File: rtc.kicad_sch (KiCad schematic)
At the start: 8 parts, among them U1501 PCF85063ATL, Y1501 32.768kHz 7pF

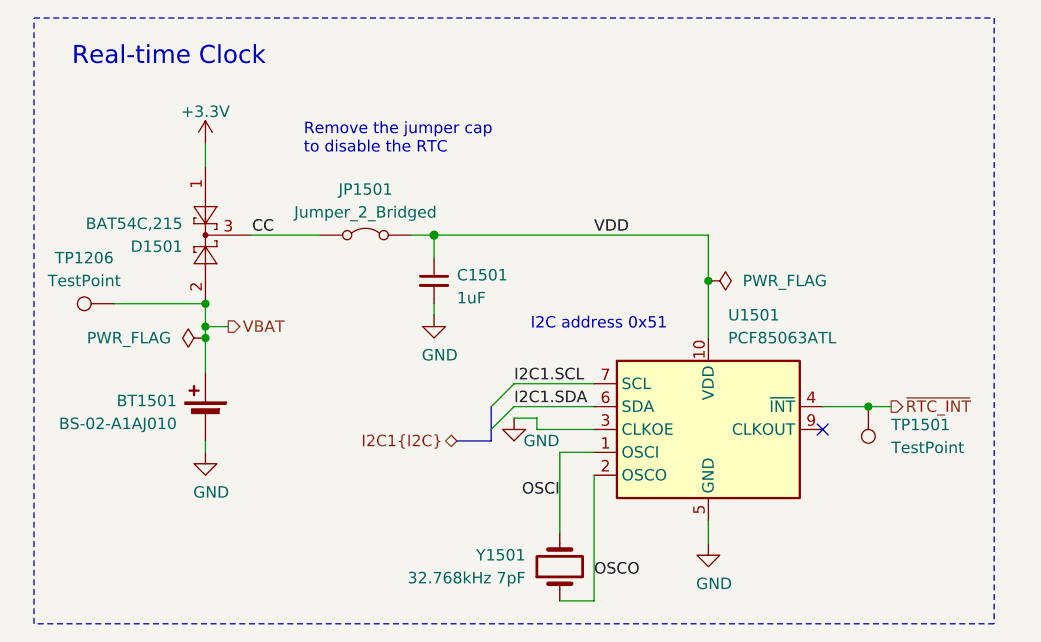
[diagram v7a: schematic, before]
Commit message: Change MCU to RP2040
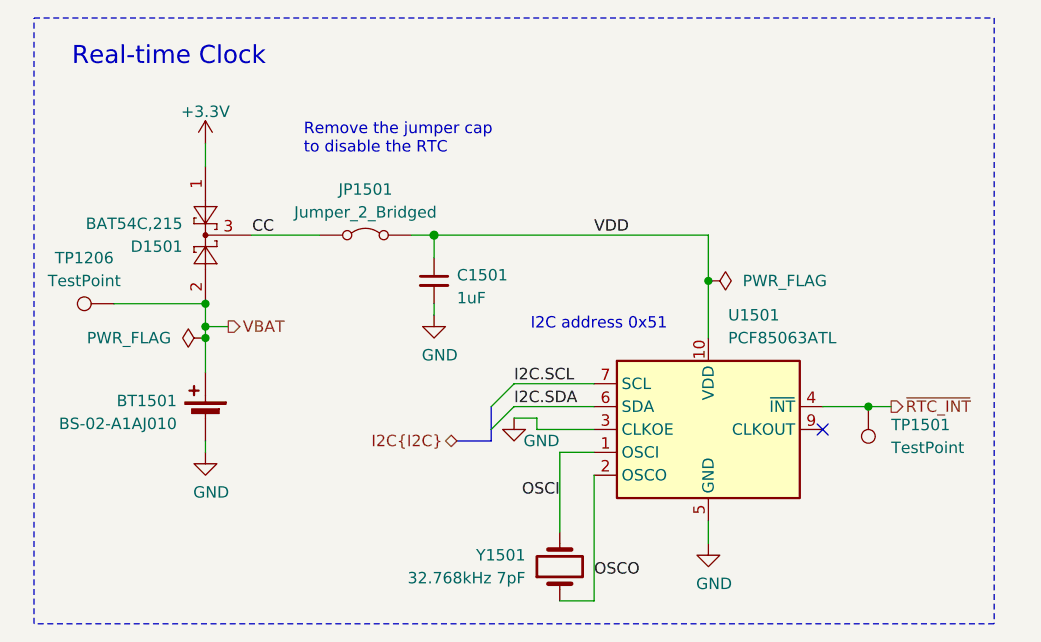
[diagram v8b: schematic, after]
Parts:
- JP1501: footprint Connector_PinHeader_2.54mm:PinHeader_1x02_P2.54mm_Vertical -> Connector_PinHeader_2.54mm:PinHeader_1x02_P2.54mm_Vertical_SMD_Pin1Left; LCSC C492401 -> C5160785
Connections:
- net I2C1.SCL renamed I2C.SCL
- net I2C1.SDA renamed I2C.SDA
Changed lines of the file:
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@@
 		)
 	)
-	(label "I2C1.SDA"
+	(label "I2C.SDA"
 		(at 146.05 101.6 0)
 		(effects
@@
 		)
 	)
-	(label "I2C1.SCL"
+	(label "I2C.SCL"
 		(at 146.05 99.06 0)
 		(effects
@@
 		)
 	)
-	(hierarchical_label "I2C1{I2C}"
+	(hierarchical_label "I2C{I2C}"
 		(shape bidirectional)
 		(at 139.7 105.41 180)
@@
 			)
 		)
-		(property "Footprint" "Connector_PinHeader_2.54mm:PinHeader_1x02_P2.54mm_Vertical"
+		(property "Footprint" "Connector_PinHeader_2.54mm:PinHeader_1x02_P2.54mm_Vertical_SMD_Pin1Left"
 			(at 129.54 82.55 0)
 			(effects
@@
 			)
 		)
-		(property "LCSC" "C492401"
+		(property "LCSC" "C5160785"
 			(at 129.54 82.55 0)
 			(effects
